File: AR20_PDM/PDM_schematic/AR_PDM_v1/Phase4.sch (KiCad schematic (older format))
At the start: 12 parts, among them Q4 BTS50025-1TAD, U10 INA233

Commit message: Alpha version DONE! - Gerber files generated
- Tweeked
- checked and re cheked
- added all missing components
- Created a really nice silkscreen
- Ready To Test
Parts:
- renumbered C_in5 to C32, C_out5 to C33, C_vs5 to C34, Cs5 to C35, C_bypass8 to C36, Q4 to Q7, R11 to R30, R_in5 to R31, R_sense5 to R32, R_s5 to R33, R_Shunt9 to R34, U10 to U7

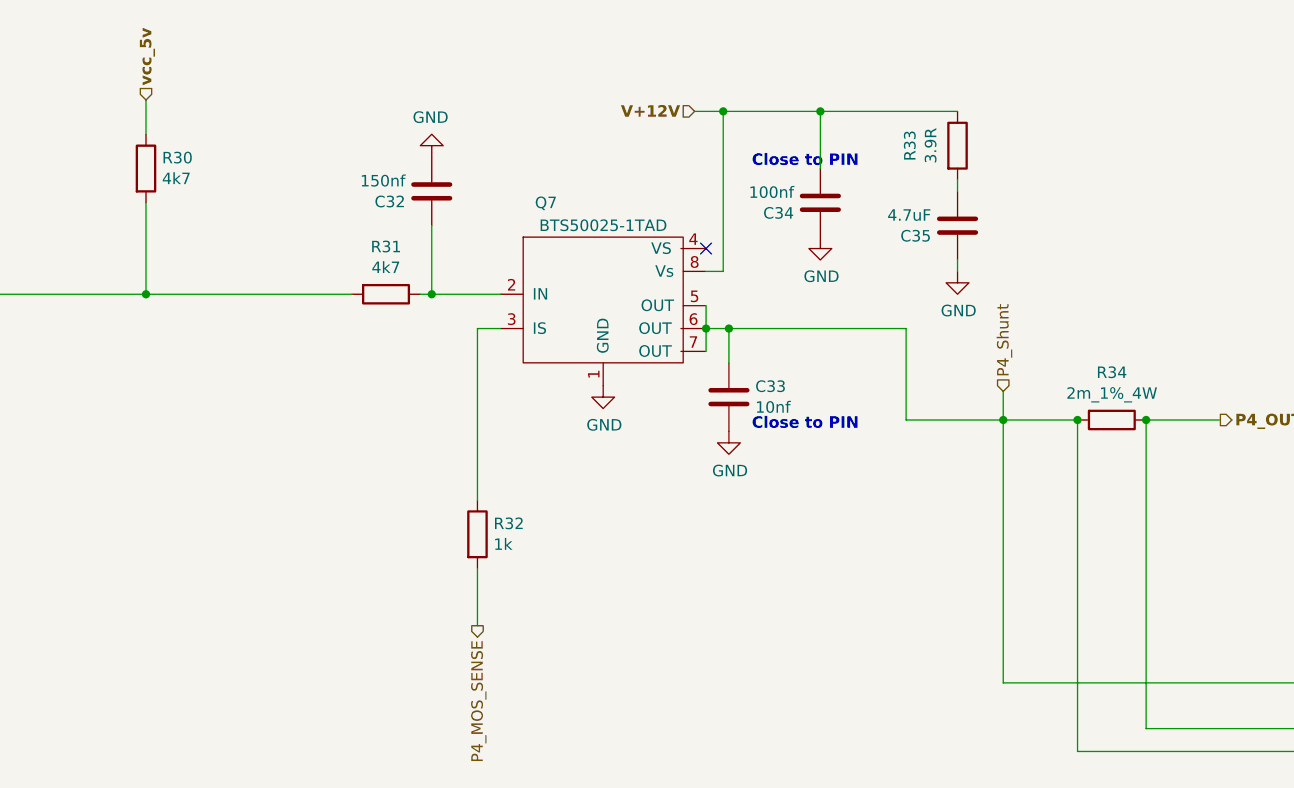
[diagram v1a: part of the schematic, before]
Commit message: Fixed wrong resistors, mos sense. Gerber files updated
- removed all R_is_protection resistors on each mosfet line
- added one R_is_protection resistors to mos_sense_all
ps, mux N-fets, does not need overvoltage protection. 60 volt tolerant.
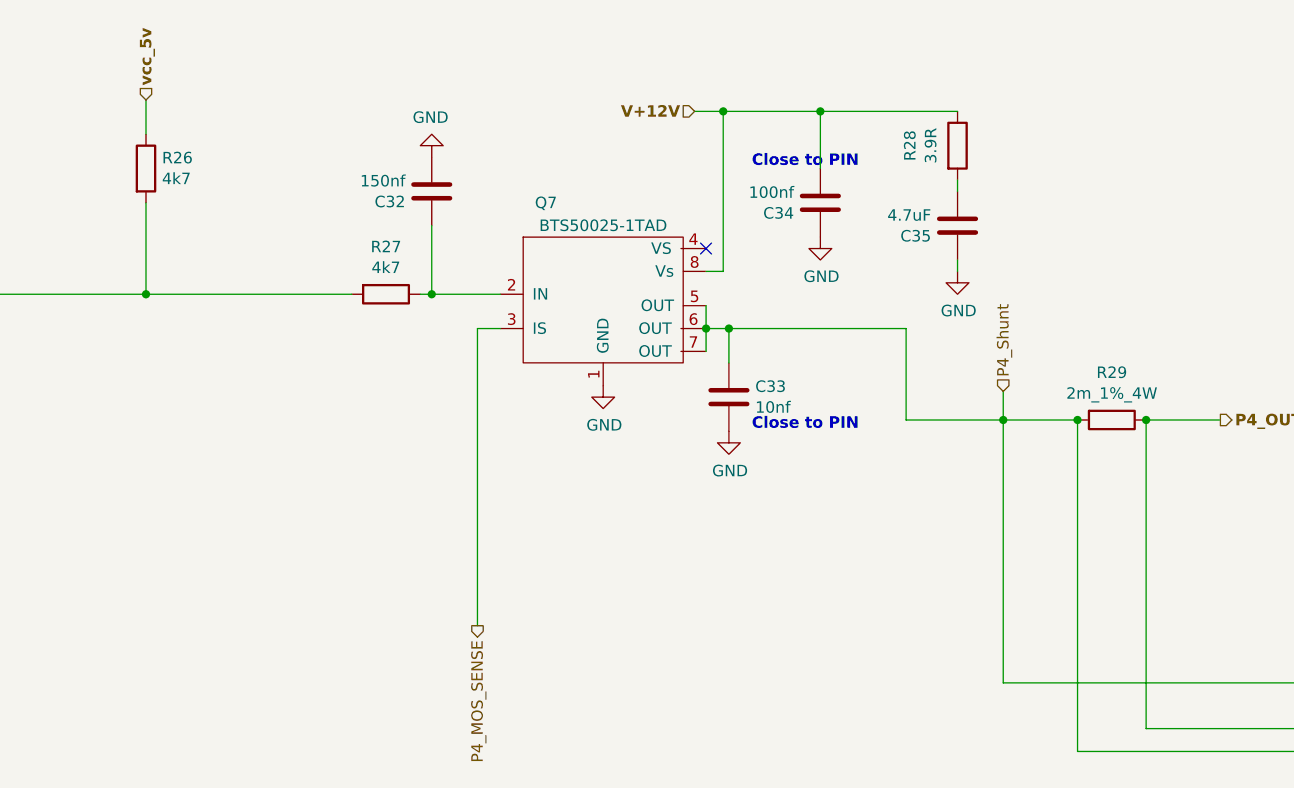
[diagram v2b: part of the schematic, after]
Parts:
- removed R32: 1k, Resistor_SMD:R_0603_1608Metric, symbol AR20_PDM_v1-rescue:R-Device
- renumbered R30 to R26, R31 to R27, R33 to R28, R34 to R29
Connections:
- net P4_MOS_SENSE: now also Q7.3 (IS)
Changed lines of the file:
@@
 AR Path="/5E0FB5C8/5E21B80B" Ref="R?"  Part="1"
 AR Path="/5E0FBBBD/5E21B80B" Ref="R?"  Part="1"
-AR Path="/5E0FC3A2/5E21B80B" Ref="R31"  Part="1"
+AR Path="/5E0FC3A2/5E21B80B" Ref="R27"  Part="1"
 AR Path="/5E0FCFDC/5E21B80B" Ref="R?"  Part="1"
 AR Path="/5E0FDCCC/5E21B80B" Ref="R?"  Part="1"
 AR Path="/5E10174B/5E21B80B" Ref="R?"  Part="1"
-F 0 "R31" V 3093 2400 50  0000 C CNN
+F 0 "R27" V 3093 2400 50  0000 C CNN
 F 1 "4k7" V 3184 2400 50  0000 C CNN
 F 2 "Resistor_SMD:R_0603_1608Metric" V 3230 2400 50  0001 C CNN
@@
 AR Path="/5E0FB5C8/5E21B81C" Ref="R?"  Part="1"
 AR Path="/5E0FBBBD/5E21B81C" Ref="R?"  Part="1"
-AR Path="/5E0FC3A2/5E21B81C" Ref="R30"  Part="1"
+AR Path="/5E0FC3A2/5E21B81C" Ref="R26"  Part="1"
 AR Path="/5E0FCFDC/5E21B81C" Ref="R?"  Part="1"
 AR Path="/5E0FDCCC/5E21B81C" Ref="R?"  Part="1"
 AR Path="/5E10174B/5E21B81C" Ref="R?"  Part="1"
-F 0 "R30" H 2320 1896 50  0000 L CNN
+F 0 "R26" H 2320 1896 50  0000 L CNN
 F 1 "4k7" H 2320 1805 50  0000 L CNN
 F 2 "Resistor_SMD:R_0603_1608Metric" V 2180 1850 50  0001 C CNN
@@
 AR Path="/5E0FB5C8/5E21B86F" Ref="R?"  Part="1"
 AR Path="/5E0FBBBD/5E21B86F" Ref="R?"  Part="1"
-AR Path="/5E0FC3A2/5E21B86F" Ref="R33"  Part="1"
+AR Path="/5E0FC3A2/5E21B86F" Ref="R28"  Part="1"
 AR Path="/5E0FCFDC/5E21B86F" Ref="R?"  Part="1"
 AR Path="/5E0FDCCC/5E21B86F" Ref="R?"  Part="1"
 AR Path="/5E10174B/5E21B86F" Ref="R?"  Part="1"
-F 0 "R33" V 5593 1750 50  0000 C CNN
+F 0 "R28" V 5593 1750 50  0000 C CNN
 F 1 "3.9R" V 5684 1750 50  0000 C CNN
 F 2 "Resistor_SMD:R_0603_1608Metric" V 5730 1750 50  0001 C CNN
@@
 Wire Wire Line
 	6000 4100 8750 4100
-$Comp
-L AR20_PDM_v1-rescue:R-Device R?
-U 1 1 5E21B877
-P 3700 3450
-AR Path="/5DA89415/5E21B877" Ref="R?"  Part="1"
-AR Path="/5DEB10A1/5E21B877" Ref="R?"  Part="1"
-AR Path="/5DEB20EA/5E21B877" Ref="R?"  Part="1"
-AR Path="/5E0E4725/5E21B877" Ref="R?"  Part="1"
-AR Path="/5E0E4A93/5E21B877" Ref="R?"  Part="1"
-AR Path="/5E0E4EB5/5E21B877" Ref="R?"  Part="1"
-AR Path="/5E0E5304/5E21B877" Ref="R?"  Part="1"
-AR Path="/5E0E594B/5E21B877" Ref="R?"  Part="1"
-AR Path="/5E0E607C/5E21B877" Ref="R?"  Part="1"
-AR Path="/5E0FB5C8/5E21B877" Ref="R?"  Part="1"
-AR Path="/5E0FBBBD/5E21B877" Ref="R?"  Part="1"
-AR Path="/5E0FC3A2/5E21B877" Ref="R32"  Part="1"
-AR Path="/5E0FCFDC/5E21B877" Ref="R?"  Part="1"
-AR Path="/5E0FDCCC/5E21B877" Ref="R?"  Part="1"
-AR Path="/5E10174B/5E21B877" Ref="R?"  Part="1"
-F 0 "R32" H 3770 3496 50  0000 L CNN
-F 1 "1k" H 3770 3405 50  0000 L CNN
-F 2 "Resistor_SMD:R_0603_1608Metric" V 3630 3450 50  0001 C CNN
-F 3 "~" H 3700 3450 50  0001 C CNN
-	1    3700 3450
-	1    0    0    -1
-$EndComp
 Wire Wire Line
 	6325 4400 8750 4400
@@
 AR Path="/5E0FB5C8/5E1D0387" Ref="R?"  Part="1"
 AR Path="/5E0FBBBD/5E1D0387" Ref="R?"  Part="1"
-AR Path="/5E0FC3A2/5E1D0387" Ref="R34"  Part="1"
+AR Path="/5E0FC3A2/5E1D0387" Ref="R29"  Part="1"
 AR Path="/5E0FCFDC/5E1D0387" Ref="R?"  Part="1"
 AR Path="/5E0FDCCC/5E1D0387" Ref="R?"  Part="1"
 AR Path="/5E10174B/5E1D0387" Ref="R?"  Part="1"
-F 0 "R34" V 6268 2950 50  0000 C CNN
+F 0 "R29" V 6268 2950 50  0000 C CNN
 F 1 "2m_1%_4W" V 6359 2950 50  0000 C CNN
 F 2 "Resistor_SMD:R_2512_6332Metric" V 6405 2950 50  0001 C CNN
@@
 Connection ~ 6000 2950
 Wire Wire Line
-	3700 3850 3700 3600
-Wire Wire Line
-	3700 2550 3700 3300
-Wire Wire Line
 	4650 1600 4775 1600
 Wire Wire Line
@@
 Wire Wire Line
 	4775 1600 5200 1600
+Wire Wire Line
+	3700 2550 3700 3850
 $EndSCHEMATC

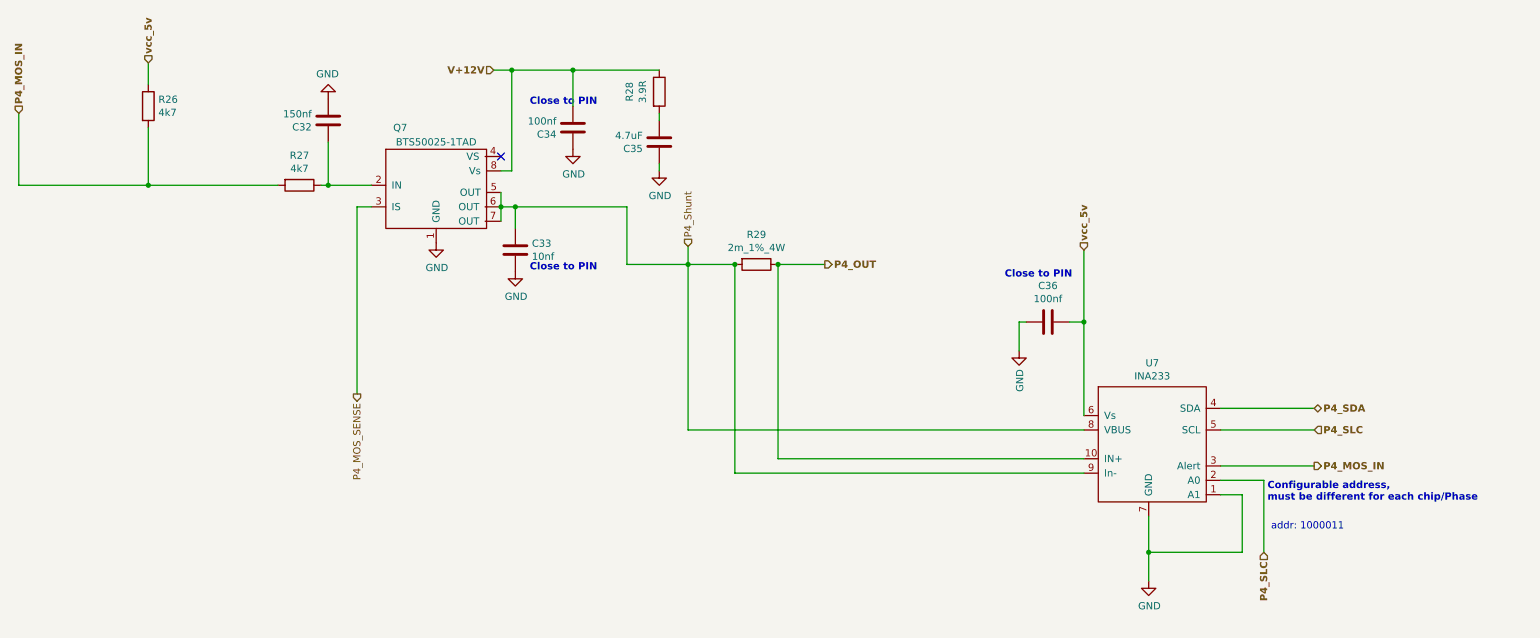
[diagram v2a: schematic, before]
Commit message: Major redesign. schematics completed, PCB work in progress
-TODO : A proper changelog file. Where all changes will apear 
- Redesigned schematics to accommodate errors in the improvement list
- More detail in ALPHA improvement list
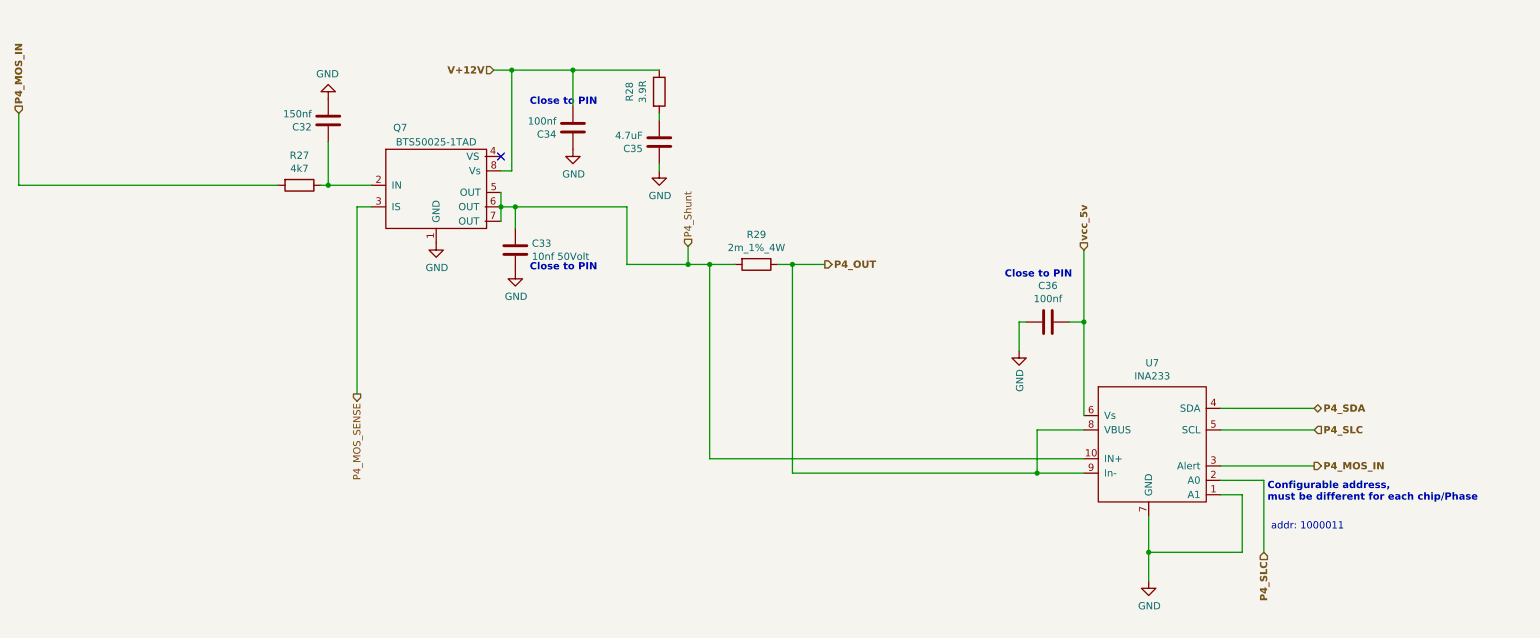
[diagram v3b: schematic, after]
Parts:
- removed R26: 4k7, Resistor_SMD:R_0603_1608Metric, symbol AR20_PDM_v1-rescue:R-Device
- C33: value 10nf -> 10nf 50Volt
- R28: footprint Resistor_SMD:R_0603_1608Metric -> Resistor_SMD:R_2512_6332Metric
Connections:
- net P4_OUT: now also U7.8 (VBUS), U7.9 (In-); no longer U7.10 (IN+)
- net P4_Shunt: now also U7.10 (IN+); no longer U7.8 (VBUS), U7.9 (In-)
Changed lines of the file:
@@
 $Descr A4 11693 8268
 encoding utf-8
-Sheet 7 13
+Sheet 7 14
 Title ""
 Date ""
@@
 AR Path="/5E10174B/5E21B811" Ref="C?"  Part="1"
 F 0 "C33" H 4915 2896 50  0000 L CNN
-F 1 "10nf" H 4915 2805 50  0000 L CNN
+F 1 "10nf 50Volt" H 4915 2805 50  0000 L CNN
 F 2 "Capacitor_SMD:C_0603_1608Metric" H 4838 2700 50  0001 C CNN
 F 3 "~" H 4800 2850 50  0001 C CNN
@@
 	-1   0    0    1
 $EndComp
-$Comp
-L AR20_PDM_v1-rescue:R-Device R?
-U 1 1 5E21B81C
-P 2250 1850
-AR Path="/5DA89415/5E21B81C" Ref="R?"  Part="1"
-AR Path="/5DEB10A1/5E21B81C" Ref="R?"  Part="1"
-AR Path="/5DEB20EA/5E21B81C" Ref="R?"  Part="1"
-AR Path="/5E0E4725/5E21B81C" Ref="R?"  Part="1"
-AR Path="/5E0E4A93/5E21B81C" Ref="R?"  Part="1"
-AR Path="/5E0E4EB5/5E21B81C" Ref="R?"  Part="1"
-AR Path="/5E0E5304/5E21B81C" Ref="R?"  Part="1"
-AR Path="/5E0E594B/5E21B81C" Ref="R?"  Part="1"
-AR Path="/5E0E607C/5E21B81C" Ref="R?"  Part="1"
-AR Path="/5E0FB5C8/5E21B81C" Ref="R?"  Part="1"
-AR Path="/5E0FBBBD/5E21B81C" Ref="R?"  Part="1"
-AR Path="/5E0FC3A2/5E21B81C" Ref="R26"  Part="1"
-AR Path="/5E0FCFDC/5E21B81C" Ref="R?"  Part="1"
-AR Path="/5E0FDCCC/5E21B81C" Ref="R?"  Part="1"
-AR Path="/5E10174B/5E21B81C" Ref="R?"  Part="1"
-F 0 "R26" H 2320 1896 50  0000 L CNN
-F 1 "4k7" H 2320 1805 50  0000 L CNN
-F 2 "Resistor_SMD:R_0603_1608Metric" V 2180 1850 50  0001 C CNN
-F 3 "~" H 2250 1850 50  0001 C CNN
-	1    2250 1850
-	1    0    0    -1
-$EndComp
 Wire Wire Line
 	4700 2550 4800 2550
@@
 Text Notes 8200 3050 0    50   ~ 10
 Close to PIN
-Text HLabel 2250 1550 1    50   Input ~ 10
-vcc_5v
 Wire Wire Line
 	9700 4100 10350 4100
-Wire Wire Line
-	2250 1550 2250 1700
 $Comp
 L AR20_PDM_v1-rescue:C-Device C?
@@
 F 0 "R28" V 5593 1750 50  0000 C CNN
 F 1 "3.9R" V 5684 1750 50  0000 C CNN
-F 2 "Resistor_SMD:R_0603_1608Metric" V 5730 1750 50  0001 C CNN
+F 2 "Resistor_SMD:R_2512_6332Metric" V 5730 1750 50  0001 C CNN
 F 3 "~" H 5800 1750 50  0001 C CNN
 	1    5800 1750
@@
 Wire Wire Line
 	9700 4350 10350 4350
-Connection ~ 2250 2400
-Wire Wire Line
-	2250 2000 2250 2400
 Wire Wire Line
 	1350 1900 1350 2400
-Wire Wire Line
-	1350 2400 2250 2400
 Wire Wire Line
 	9200 4950 9200 5150
@@
 	5575 2550 5575 2950
 Connection ~ 4800 2550
-Wire Wire Line
-	6000 4100 8750 4100
-Wire Wire Line
-	6325 4400 8750 4400
-Wire Wire Line
-	6625 4300 8750 4300
 Text HLabel 3700 3850 3    50   Output ~ 0
 P4_MOS_SENSE
-Wire Wire Line
-	6000 4100 6000 2950
 Wire Wire Line
 	5575 2950 6000 2950
@@
 Text HLabel 4650 1600 0    50   Input ~ 10
 V+12V
-Wire Wire Line
-	2250 2400 3150 2400
 $Comp
 L AR20_PDM_v1-rescue:C-Device C?
@@
 $EndComp
 Wire Wire Line
-	6625 2950 6625 4300
-Wire Wire Line
-	6325 2950 6325 4400
-Wire Wire Line
-	6000 2950 6325 2950
+	6000 2950 6150 2950
 $Comp
 L AR20_PDM_v1-rescue:R-Device R?
@@
 $EndComp
 Wire Wire Line
-	6625 2950 6950 2950
-Connection ~ 6325 2950
-Connection ~ 6625 2950
+	6625 2950 6725 2950
 Text Notes 10050 4800 0    50   ~ 0
 addr: 1000011
@@
 Wire Wire Line
 	3700 2550 3700 3850
+Wire Wire Line
+	1350 2400 3150 2400
+Wire Wire Line
+	8750 4300 6150 4300
+Wire Wire Line
+	6150 4300 6150 2950
+Wire Wire Line
+	8750 4400 8425 4400
+Wire Wire Line
+	6725 4400 6725 2950
+Wire Wire Line
+	8750 4100 8425 4100
+Wire Wire Line
+	8425 4100 8425 4400
+Connection ~ 8425 4400
+Wire Wire Line
+	8425 4400 6725 4400
+Connection ~ 6725 2950
+Wire Wire Line
+	6725 2950 6950 2950
+Connection ~ 6150 2950
+Wire Wire Line
+	6150 2950 6325 2950
 $EndSCHEMATC

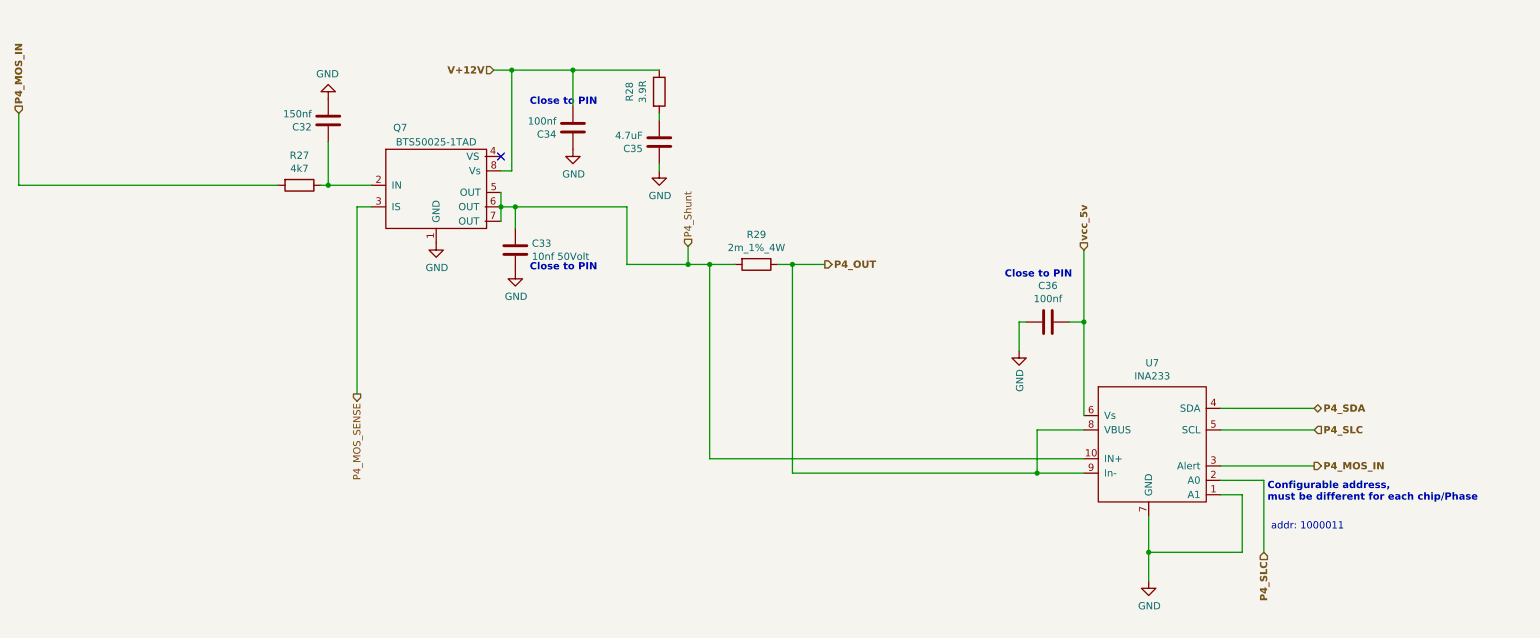
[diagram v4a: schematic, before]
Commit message: schematics rework
Fixed INA233 frying due to inductive flyback:
- Paced ina233 high side of the mosftets
- New input protection reseistors, and zener diodes, on each ina233.
Simplified:
- Removed the MUX and mos sense lines, as i realize that most of this functionality can be obtained trough INA233.
- Removed some of the cappacitors , besides the most needed ones.
- removed  back to back zener diode configuration, now a single diode insted.
 to reduce negative voltage in case of loss of VS, to be easy on the INA233 filters.
new stuff:
- Another temp sensor.
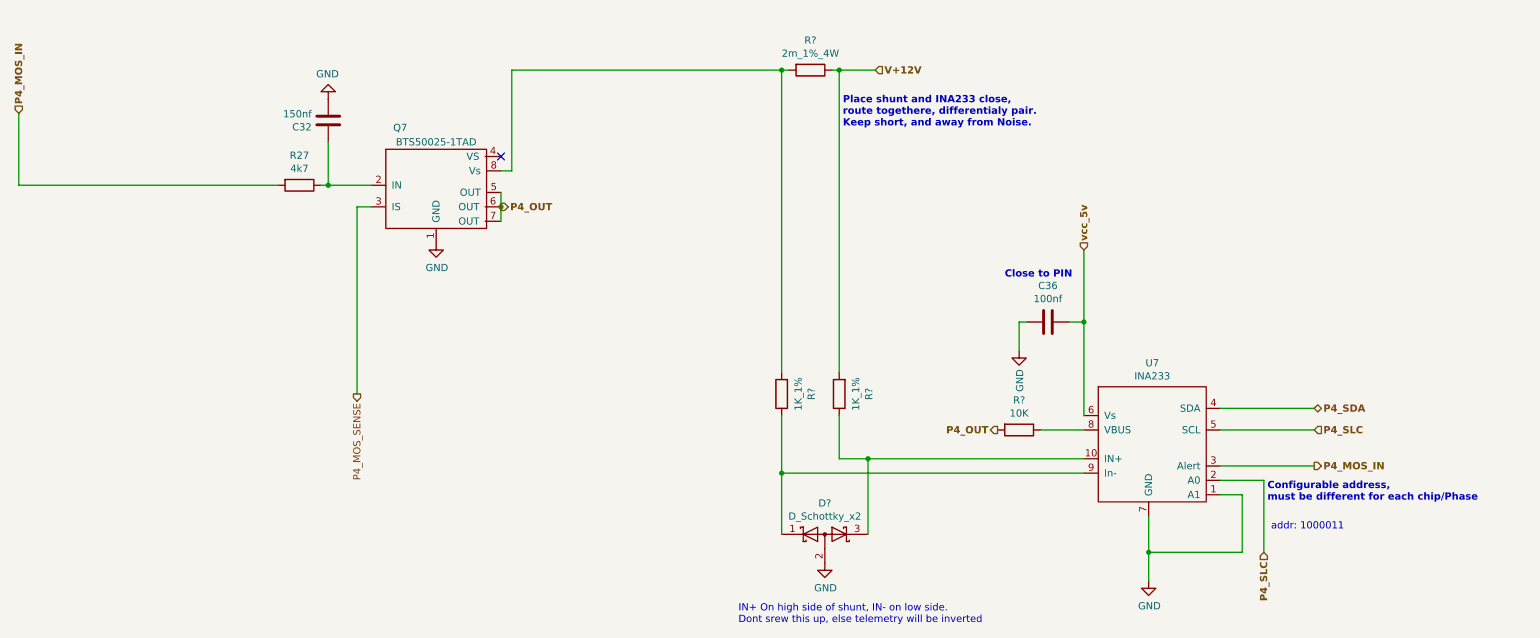
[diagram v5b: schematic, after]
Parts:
- removed C33: 10nf 50Volt, Capacitor_SMD:C_0603_1608Metric, symbol AR20_PDM_v1-rescue:C-Device
- removed C34: 100nf, Capacitor_SMD:C_0603_1608Metric, symbol AR20_PDM_v1-rescue:C-Device
- removed C35: 4.7uF, Capacitor_SMD:C_1206_3216Metric, symbol AR20_PDM_v1-rescue:C-Device
- removed R28: 3.9R, Resistor_SMD:R_2512_6332Metric, symbol AR20_PDM_v1-rescue:R-Device
- removed R29: 2m_1%_4W, Resistor_SMD:R_2512_6332Metric, symbol AR20_PDM_v1-rescue:R-Device
- added D?: D_Schottky_x2, symbol AR20_PDM_v1-rescue:D_Schottky_x2
- added R?: 2m_1%_4W, Resistor_SMD:R_2512_6332Metric, symbol AR20_PDM_v1-rescue:R-Device
- added R? (x2): 1K_1%, Resistor_SMD:R_0603_1608Metric, symbol AR20_PDM_v1-rescue:R-Device
- added R?: 10K, Resistor_SMD:R_0603_1608Metric, symbol AR20_PDM_v1-rescue:R-Device
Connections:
- net GND: now also D?.2 (A)
- net P4_OUT: now also Q7.5 (OUT), Q7.6 (OUT), Q7.7 (OUT), R?.2; no longer U7.8 (VBUS), U7.9 (In-)
- net V+12V: now also R?.1, R?.2; no longer Q7.8 (Vs)
- removed net P4_Shunt: Q7.5 (OUT), Q7.6 (OUT), Q7.7 (OUT), U7.10 (IN+)
- new net: Q7.8 (Vs), R?.2, R?.2
- new net: D?.3 (K), R?.1, U7.10 (IN+)
- new net: R?.1, U7.8 (VBUS)
- new net: D?.1 (K), R?.1, U7.9 (In-)
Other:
- note added: "IN+ On high side of shunt, IN- on low side.\nDont srew this up, else telemetry will be inverted"
- note added: "Place shunt and INA233 close, \nroute togethere, differentialy pair. \nKeep short, and away from Noise."
